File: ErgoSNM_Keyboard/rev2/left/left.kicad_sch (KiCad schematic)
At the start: 27 parts, among them J1 USB_C_Receptacle_USB2.0, J2 Conn_01x10, Q1 BSS138, U1 SRV05-4, U2 RT9013-33GB

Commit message: Update rev2
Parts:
- removed C3: 100nF, Capacitor_SMD:C_0402_1005Metric, symbol Device:C
- removed H4, H7, H9: MountingHole, MountingHole:MountingHole_2.2mm_M2, symbol Mechanical:MountingHole
- removed J2: Conn_01x10, Connector_PinSocket_2.54mm:PinSocket_1x10_P2.54mm_Vertical, symbol Connector_Generic:Conn_01x10
- removed LD1: SK6812MINI-E, ErgoSNM_Keyboard:SK6812MINI-E, symbol ErgoSNM_Keyboard_Library:SK6812MINI-E
- removed Q1: BSS138, Package_TO_SOT_SMD:SOT-23, symbol Transistor_FET:BSS138
- removed R3, R4: 10k, Resistor_SMD:R_0402_1005Metric, symbol Device:R
- removed TP3: TestPoint, TestPoint:TestPoint_Pad_D2.0mm, symbol Connector:TestPoint
- added J2: Conn_01x10, Connector_PinSocket_2.54mm:PinSocket_1x08_P2.54mm_Vertical, symbol Connector_Generic:Conn_01x08
- renumbered H8 to H4
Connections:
- net +3V3: now also J2.1 (Pin_1)
- net CS: now also J2.3 (Pin_3)
- net Encoder_A: now also J2.8 (Pin_8)
- net Encoder_B: now also J2.7 (Pin_7)
- net GND: now also J2.2 (Pin_2)
- net MISO: now also J2.5 (Pin_5)
- net MOSI: now also J2.4 (Pin_4)
- net SCLK: now also J2.6 (Pin_6)

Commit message: Update BOM, net, placement, etc.
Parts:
- removed J2: Conn_01x10, Connector_PinSocket_2.54mm:PinSocket_1x08_P2.54mm_Vertical, symbol Connector_Generic:Conn_01x08
- added J2: USB_C_Receptacle_USB2.0, Connector_USB:USB_C_Receptacle_HRO_TYPE-C-31-M-12, symbol Connector:USB_C_Receptacle_USB2.0
- added J4: Conn_01x08, Connector_JST:JST_GH_SM08B-GHS-TB_1x08-1MP_P1.25mm_Horizontal, symbol Connector_Generic:Conn_01x08
- added LD1: Red, LED_SMD:LED_0603_1608Metric, symbol Device:LED
- added R3: 1k, Resistor_SMD:R_0402_1005Metric, symbol Device:R
- added TP1, TP4: TestPoint, TestPoint:TestPoint_Pad_D2.5mm, symbol Connector:TestPoint
- C1, C2: JLCPCB Part # C52923 -> (none); LCSC (none) -> C52923
- F1: JLCPCB Part # C269104 -> (none); LCSC (none) -> C269104
- J1: JLCPCB Part # C165948 -> (none); LCSC (none) -> C165948
- J3: renamed from TRRS1; footprint ErgoSNM_Keyboard:PJ-393 -> ErgoSNM_Keyboard:PJ-393 8P TRRS; LCSC (none) -> C668609; MFR. Part # (none) -> PJ-393 8PJ
- R1, R2: JLCPCB Part # C25905 -> (none); LCSC (none) -> C25905
- TP2: renamed from TP1; now left out of the parts list
- TP3: renamed from TP2; now left out of the parts list
- U1: renamed from U2; JLCPCB Part # C47773 -> (none); LCSC (none) -> C47773
- U2: renamed from U1; LCSC (none) -> C85364; MFR. Part # (none) -> SRV05-4-P-T7
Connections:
- net +3V3: now also J3.S, J2.A4 (VBUS), J2.A9 (VBUS), J2.B4 (VBUS), J2.B9 (VBUS), TP1.1
- net +5V: no longer J3.8 (Sa)
- net Encoder_A: now also J4.6 (Pin_6)
- net Encoder_B: now also J4.7 (Pin_7)
- net GND: now also J3.T, J2.A1 (GND), J2.A12 (GND), J2.B1 (GND), J2.B12 (GND), J2.S1 (SHIELD), J4.8 (Pin_8), R3.2, TP4.1; no longer J3.1 (Ta)
- net SERIAL: now also J3.R1, J2.A6 (D+), J2.B6 (D+); no longer J3.2 (R1a)
- new net: LD1.1 (K), R3.1
- new net COL_5: J4.1 (Pin_1)
- new net COL_6: J4.5 (Pin_5)
- new net COL_7: J4.4 (Pin_4)
- new net ROW_4: J4.2 (Pin_2)
- new net ROW_5: J4.3 (Pin_3)
- new net STATE_LED: LD1.2 (A)
- no-connect marks 7 -> 15
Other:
- note added: "Main"
- note added: "Power"
- note added: "Split Communication"
- note added: "USB"
- note added: "USB ESD Protection"
- moved on the sheet: C1, C2, F1, J1, R1, R2, TP2, TP3, U1, U2

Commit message: Replace JST GH 1.25 connector with 0.5mm FPC
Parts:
- J4: footprint Connector_JST:JST_GH_SM08B-GHS-TB_1x08-1MP_P1.25mm_Horizontal -> ErgoSNM_Keyboard:FPC_8P_0.5mm_AFC01-S08FCA-00
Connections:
- net COL_5: now also J4.8 (Pin_8); no longer J4.1 (Pin_1)
- net COL_6: now also J4.4 (Pin_4); no longer J4.5 (Pin_5)
- net COL_7: now also J4.5 (Pin_5); no longer J4.4 (Pin_4)
- net Encoder_A: now also J4.3 (Pin_3); no longer J4.6 (Pin_6)
- net Encoder_B: now also J4.2 (Pin_2); no longer J4.7 (Pin_7)
- net GND: now also J4.1 (Pin_1); no longer J4.8 (Pin_8)
- net ROW_4: now also J4.7 (Pin_7); no longer J4.2 (Pin_2)
- net ROW_5: now also J4.6 (Pin_6); no longer J4.3 (Pin_3)
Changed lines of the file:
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@@
   (title_block
     (title "ErgoSNM Keyboard - Left")
-    (rev "2.0")
+    (rev "2.1")
     (comment 1 "MIT License (Open source hardware)")
     (comment 2 "https://github.com/ziteh/ergo-snm-keyboard")
@@
     (pin "1")
   )
-  (symbol (lib_id "Connector_Generic:Conn_01x08") (at 138.43 166.37 0) (unit 1)
+  (symbol (lib_id "Connector_Generic:Conn_01x08") (at 138.43 168.91 0) (mirror x) (unit 1)
     (in_bom yes) (on_board yes) (fields_autoplaced)
-    (property "Reference" "J4" (id 0) (at 140.97 166.3699 0)
-      (effects (font (size 1.27 1.27)) (justify left))
-    )
-    (property "Value" "Conn_01x08" (id 1) (at 140.97 168.9099 0)
-      (effects (font (size 1.27 1.27)) (justify left))
-    )
-    (property "Footprint" "Connector_JST:JST_GH_SM08B-GHS-TB_1x08-1MP_P1.25mm_Horizontal" (id 2) (at 138.43 166.37 0)
-      (effects (font (size 1.27 1.27)) hide)
-    )
-    (property "Datasheet" "~" (id 3) (at 138.43 166.37 0)
-      (effects (font (size 1.27 1.27)) hide)
-    )
-    (property "LCSC" "C265111" (id 4) (at 138.43 166.37 0)
-      (effects (font (size 1.27 1.27)) hide)
-    )
-    (property "MFR. Part #" "SM08B-GHS-TB(LF)(SN)" (id 5) (at 138.43 166.37 0)
+    (property "Reference" "J4" (id 0) (at 138.43 152.4 0))
+    (property "Value" "Conn_01x08" (id 1) (at 138.43 154.94 0))
+    (property "Footprint" "ErgoSNM_Keyboard:FPC_8P_0.5mm_AFC01-S08FCA-00" (id 2) (at 138.43 168.91 0)
+      (effects (font (size 1.27 1.27)) hide)
+    )
+    (property "Datasheet" "~" (id 3) (at 138.43 168.91 0)
+      (effects (font (size 1.27 1.27)) hide)
+    )
+    (property "LCSC" "C265111" (id 4) (at 138.43 168.91 0)
+      (effects (font (size 1.27 1.27)) hide)
+    )
+    (property "MFR. Part #" "SM08B-GHS-TB(LF)(SN)" (id 5) (at 138.43 168.91 0)
       (effects (font (size 1.27 1.27)) hide)
     )
@@
     )
     (path "/d0686554-530b-491a-bdc9-ed48c45d810a"
-      (reference "J4") (unit 1) (value "Conn_01x08") (footprint "Connector_JST:JST_GH_SM08B-GHS-TB_1x08-1MP_P1.25mm_Horizontal")
+      (reference "J4") (unit 1) (value "Conn_01x08") (footprint "ErgoSNM_Keyboard:FPC_8P_0.5mm_AFC01-S08FCA-00")
     )
     (path "/1a54857c-0204-45b8-b08f-47236e02c723/bef0ed30-218e-42e5-9109-965e80a536d2"

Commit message: Add additional LED and upadrte LED position
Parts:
- added LD2: LED, LED_SMD:LED_0805_2012Metric_Pad1.15x1.40mm_HandSolder, symbol Device:LED
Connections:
- net STATE_LED: now also LD2.2 (A)
- net at LD1.1 (K), R3.1: now also LD2.1 (K)
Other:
- moved on the sheet: R3
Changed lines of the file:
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@@
   (junction (at 55.88 44.45) (diameter 0) (color 0 0 0 0)
   )
+  (junction (at 60.96 168.91) (diameter 0) (color 0 0 0 0)
+  )
   (junction (at 241.3 43.18) (diameter 0) (color 0 0 0 0)
   )
   (junction (at 55.88 49.53) (diameter 0) (color 0 0 0 0)
+  )
+  (junction (at 53.34 157.48) (diameter 0) (color 0 0 0 0)
   )
   (junction (at 212.09 43.18) (diameter 0) (color 0 0 0 0)
@@
     (stroke (width 0) (type default) (color 0 0 0 0))
   )
+  (wire (pts (xy 53.34 168.91) (xy 60.96 168.91))
+    (stroke (width 0) (type default) (color 0 0 0 0))
+  )
   (polyline (pts (xy 176.53 12.7) (xy 176.53 165.1))
     (stroke (width 0) (type default) (color 0 0 0 0))
@@
     (stroke (width 0) (type default) (color 0 0 0 0))
   )
+  (wire (pts (xy 60.96 168.91) (xy 67.31 168.91))
+    (stroke (width 0) (type default) (color 0 0 0 0))
+  )
   (wire (pts (xy 71.12 38.1) (xy 67.31 38.1))
     (stroke (width 0) (type default) (color 0 0 0 0))
@@
     (stroke (width 0) (type default) (color 0 0 0 0))
   )
+  (wire (pts (xy 53.34 157.48) (xy 67.31 157.48))
+    (stroke (width 0) (type default) (color 0 0 0 0))
+  )
   (wire (pts (xy 54.61 48.26) (xy 55.88 48.26))
     (stroke (width 0) (type default) (color 0 0 0 0))
@@
     (stroke (width 0) (type default) (color 0 0 0 0))
   )
+  (wire (pts (xy 67.31 158.75) (xy 67.31 157.48))
+    (stroke (width 0) (type default) (color 0 0 0 0))
+  )
   (wire (pts (xy 241.3 43.18) (xy 241.3 45.72))
     (stroke (width 0) (type default) (color 0 0 0 0))
@@
     (stroke (width 0) (type default) (color 0 0 0 0))
   )
-  (wire (pts (xy 53.34 168.91) (xy 53.34 166.37))
-    (stroke (width 0) (type default) (color 0 0 0 0))
-  )
   (wire (pts (xy 217.17 133.35) (xy 218.44 133.35))
     (stroke (width 0) (type default) (color 0 0 0 0))
@@
   )
   (wire (pts (xy 29.21 114.3) (xy 38.1 114.3))
+    (stroke (width 0) (type default) (color 0 0 0 0))
+  )
+  (wire (pts (xy 53.34 166.37) (xy 53.34 168.91))
+    (stroke (width 0) (type default) (color 0 0 0 0))
+  )
+  (wire (pts (xy 67.31 166.37) (xy 67.31 168.91))
     (stroke (width 0) (type default) (color 0 0 0 0))
   )
@@
     (pin "1")
   )
+  (symbol (lib_id "Device:LED") (at 67.31 162.56 90) (unit 1)
+    (in_bom yes) (on_board yes) (fields_autoplaced)
+    (property "Reference" "LD2" (id 0) (at 71.12 162.8774 90)
+      (effects (font (size 1.27 1.27)) (justify right))
+    )
+    (property "Value" "LED" (id 1) (at 71.12 165.4174 90)
+      (effects (font (size 1.27 1.27)) (justify right))
+    )
+    (property "Footprint" "LED_SMD:LED_0805_2012Metric_Pad1.15x1.40mm_HandSolder" (id 2) (at 67.31 162.56 0)
+      (effects (font (size 1.27 1.27)) hide)
+    )
+    (property "Datasheet" "~" (id 3) (at 67.31 162.56 0)
+      (effects (font (size 1.27 1.27)) hide)
+    )
+    (pin "1")
+    (pin "2")
+  )
   (symbol (lib_id "power:GND") (at 245.11 147.32 0) (unit 1)
     (in_bom yes) (on_board yes)
@@
     (pin "1")
   )
-  (symbol (lib_id "power:GND") (at 53.34 176.53 0) (unit 1)
-    (in_bom yes) (on_board yes)
-    (property "Reference" "#PWR019" (id 0) (at 53.34 182.88 0)
-      (effects (font (size 1.27 1.27)) hide)
-    )
-    (property "Value" "GND" (id 1) (at 53.34 180.34 0))
-    (property "Footprint" "" (id 2) (at 53.34 176.53 0)
-      (effects (font (size 1.27 1.27)) hide)
-    )
-    (property "Datasheet" "" (id 3) (at 53.34 176.53 0)
+  (symbol (lib_id "power:GND") (at 60.96 176.53 0) (unit 1)
+    (in_bom yes) (on_board yes)
+    (property "Reference" "#PWR019" (id 0) (at 60.96 182.88 0)
+      (effects (font (size 1.27 1.27)) hide)
+    )
+    (property "Value" "GND" (id 1) (at 60.96 180.34 0))
+    (property "Footprint" "" (id 2) (at 60.96 176.53 0)
+      (effects (font (size 1.27 1.27)) hide)
+    )
+    (property "Datasheet" "" (id 3) (at 60.96 176.53 0)
       (effects (font (size 1.27 1.27)) hide)
     )
@@
     (pin "1")
   )
-  (symbol (lib_id "Device:R") (at 53.34 172.72 0) (mirror y) (unit 1)
-    (in_bom yes) (on_board yes)
-    (property "Reference" "R3" (id 0) (at 55.88 171.45 0)
+  (symbol (lib_id "Device:R") (at 60.96 172.72 0) (mirror y) (unit 1)
+    (in_bom yes) (on_board yes)
+    (property "Reference" "R3" (id 0) (at 63.5 171.45 0)
       (effects (font (size 1.27 1.27)) (justify right))
     )
-    (property "Value" "1k" (id 1) (at 55.88 173.99 0)
+    (property "Value" "1k" (id 1) (at 63.5 173.99 0)
       (effects (font (size 1.27 1.27)) (justify right))
     )
-    (property "Footprint" "Resistor_SMD:R_0402_1005Metric" (id 2) (at 55.118 172.72 90)
-      (effects (font (size 1.27 1.27)) hide)
-    )
-    (property "Datasheet" "~" (id 3) (at 53.34 172.72 0)
-      (effects (font (size 1.27 1.27)) hide)
-    )
-    (property "MFR. Part #" "0402WGF1001TCE " (id 4) (at 53.34 172.72 0)
-      (effects (font (size 1.27 1.27)) hide)
-    )
-    (property "JLCPCB Part #" "" (id 5) (at 53.34 172.72 0)
-      (effects (font (size 1.27 1.27)) hide)
-    )
-    (property "LCSC" "C11702" (id 6) (at 53.34 172.72 0)
+    (property "Footprint" "Resistor_SMD:R_0402_1005Metric" (id 2) (at 62.738 172.72 90)
+      (effects (font (size 1.27 1.27)) hide)
+    )
+    (property "Datasheet" "~" (id 3) (at 60.96 172.72 0)
+      (effects (font (size 1.27 1.27)) hide)
+    )
+    (property "MFR. Part #" "0402WGF1001TCE " (id 4) (at 60.96 172.72 0)
+      (effects (font (size 1.27 1.27)) hide)
+    )
+    (property "JLCPCB Part #" "" (id 5) (at 60.96 172.72 0)
+      (effects (font (size 1.27 1.27)) hide)
+    )
+    (property "LCSC" "C11702" (id 6) (at 60.96 172.72 0)
       (effects (font (size 1.27 1.27)) hide)
     )
@@
       (reference "LD1") (unit 1) (value "Red") (footprint "LED_SMD:LED_0603_1608Metric")
     )
+    (path "/42d51516-9c7f-4d58-8951-cf906b1c43d0"
+      (reference "LD2") (unit 1) (value "LED") (footprint "LED_SMD:LED_0805_2012Metric_Pad1.15x1.40mm_HandSolder")
+    )
     (path "/52df35e2-c9f1-4800-bc19-8e21e90aab38"

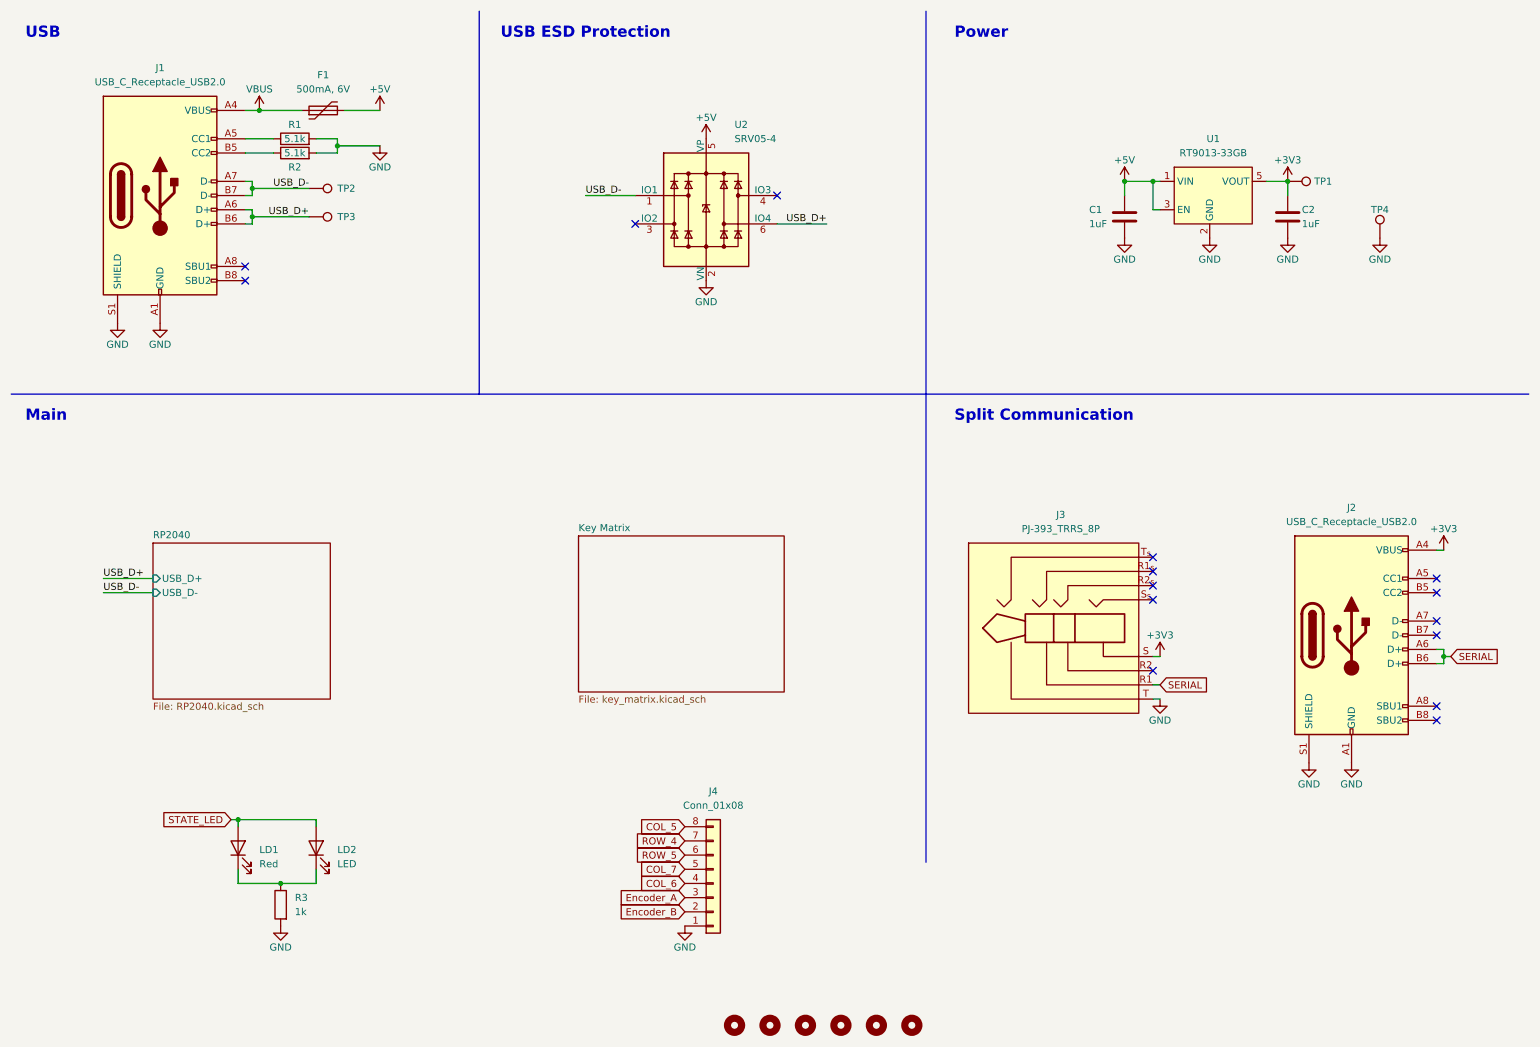
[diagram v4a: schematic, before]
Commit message: Change license to CERN-OHL-P v2
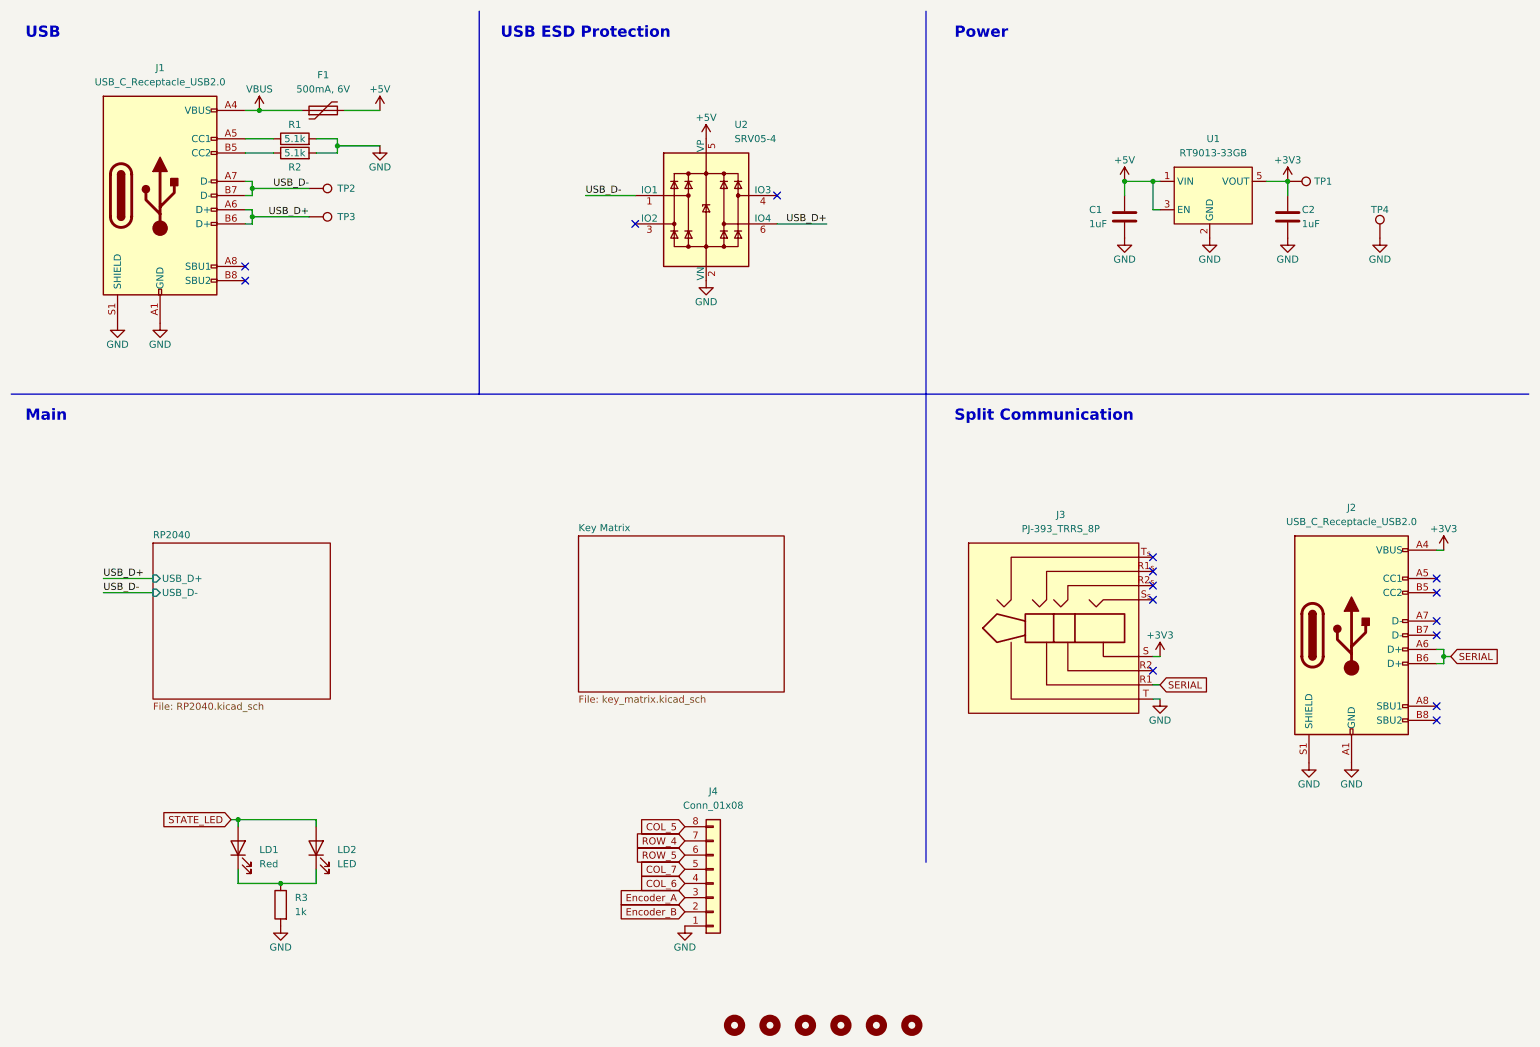
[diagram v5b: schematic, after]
